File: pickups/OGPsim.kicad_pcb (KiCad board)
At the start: 2 copper layers, 6 parts, among them Q3 QSB363, Q4 QSB363

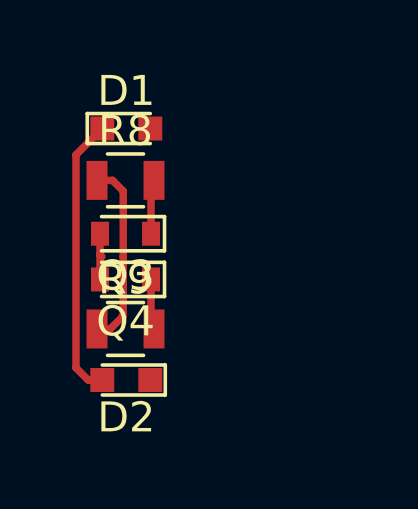
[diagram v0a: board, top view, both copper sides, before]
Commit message: Added solder pads to pickup and adjusted placement of solder pads on demodulator.
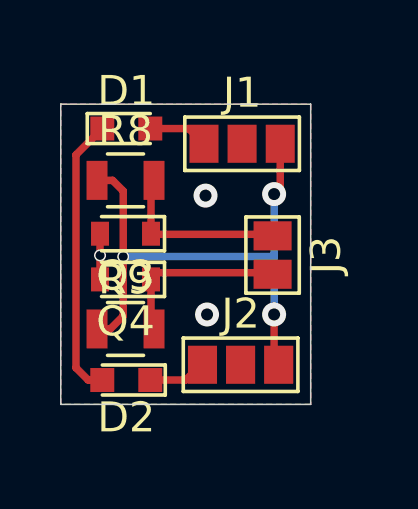
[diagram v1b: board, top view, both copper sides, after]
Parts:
- added J1: Conn_01x03, Connect:GS3, F.Cu at (144.7, 99.2)
- added J2: Conn_01x03, Connect:GS3, F.Cu at (144.7, 106.6)
- added J3: Conn_01x02_MountingPin, Connect:GS2, F.Cu at (145.7, 102.9)
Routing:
- net +9V: track 6.24 -> 18.8 mm, vias 0 -> 3
- net Net-(J3-Pad2): track 1.71 -> 5.80 mm
- net Net-(J3-Pad1): track 1.82 -> 5.83 mm
- net Net-(D1-Pad2): track 0.00 -> 2.00 mm
- net Net-(D2-Pad1): track 0.00 -> 1.97 mm
- net GND: vias 0 -> 3
- added copper zone on B.Cu, net GND
- added copper zone on F.Cu, net GND
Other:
- board outline added: 8.3 x 10 mm

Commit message: Cleaned up silk screen layers and moved part REFs to UserDrawings. Made PNG image file of part REFs for Power Supply and Pickup Boards.
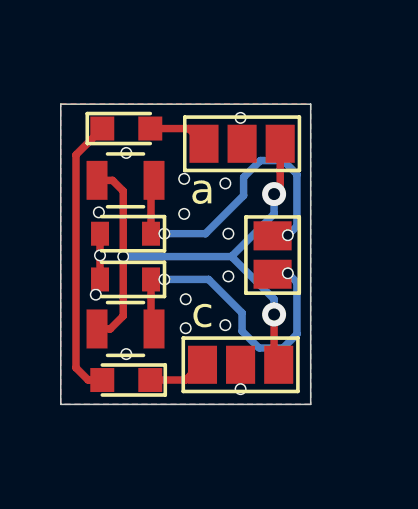
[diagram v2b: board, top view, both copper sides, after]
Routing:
- net Net-(J3-Pad1): track 5.83 -> 10.4 mm, vias 0 -> 2
- net Net-(J3-Pad2): track 5.80 -> 10.2 mm, vias 0 -> 2
- net GND: vias 3 -> 15
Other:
- board text added: "a"
- board text added: "c"
